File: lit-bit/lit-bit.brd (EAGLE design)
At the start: 8.1 x 1.3 mm, 10 parts, among them IC1 ATMEGA32U4-MU, SW1 SPST_TACT-KMR2, U1 S-1317A33-M5T1U4, X3 microUSB, Y1 8MHz

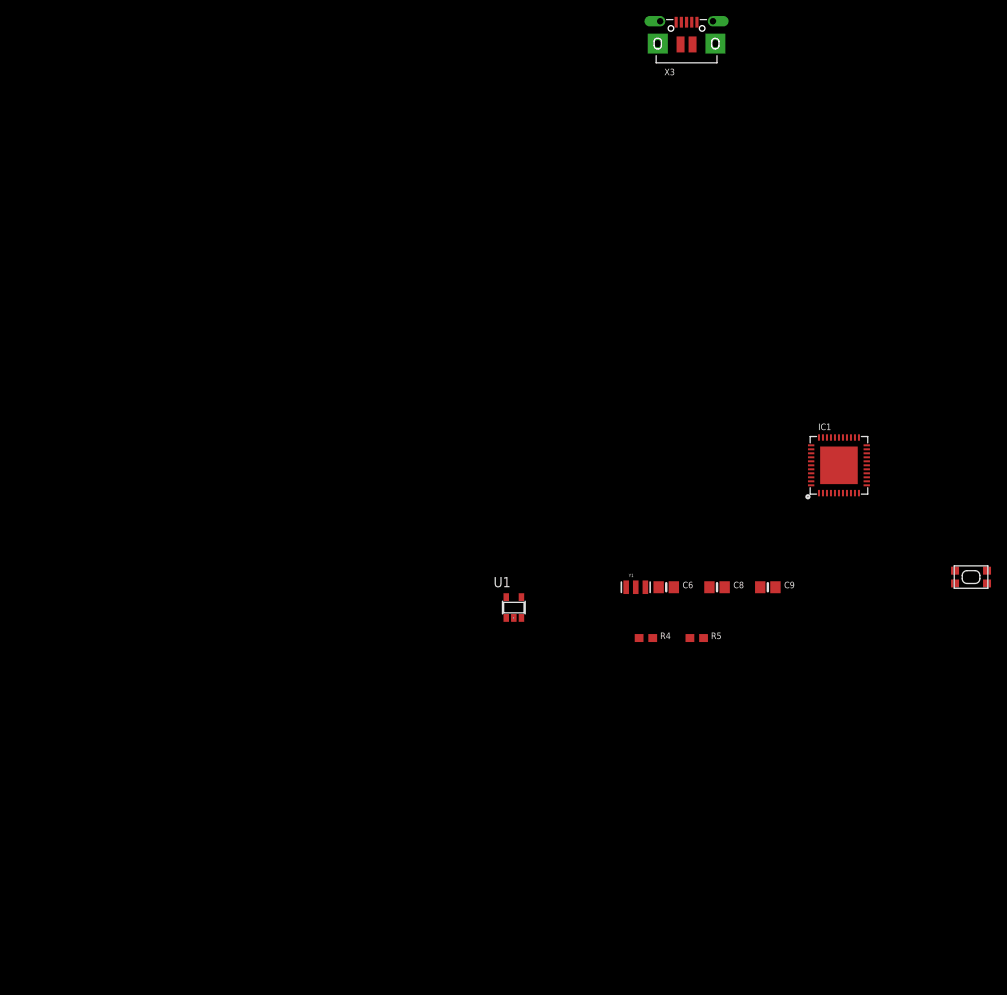
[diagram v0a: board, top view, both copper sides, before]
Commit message: added power circuitry
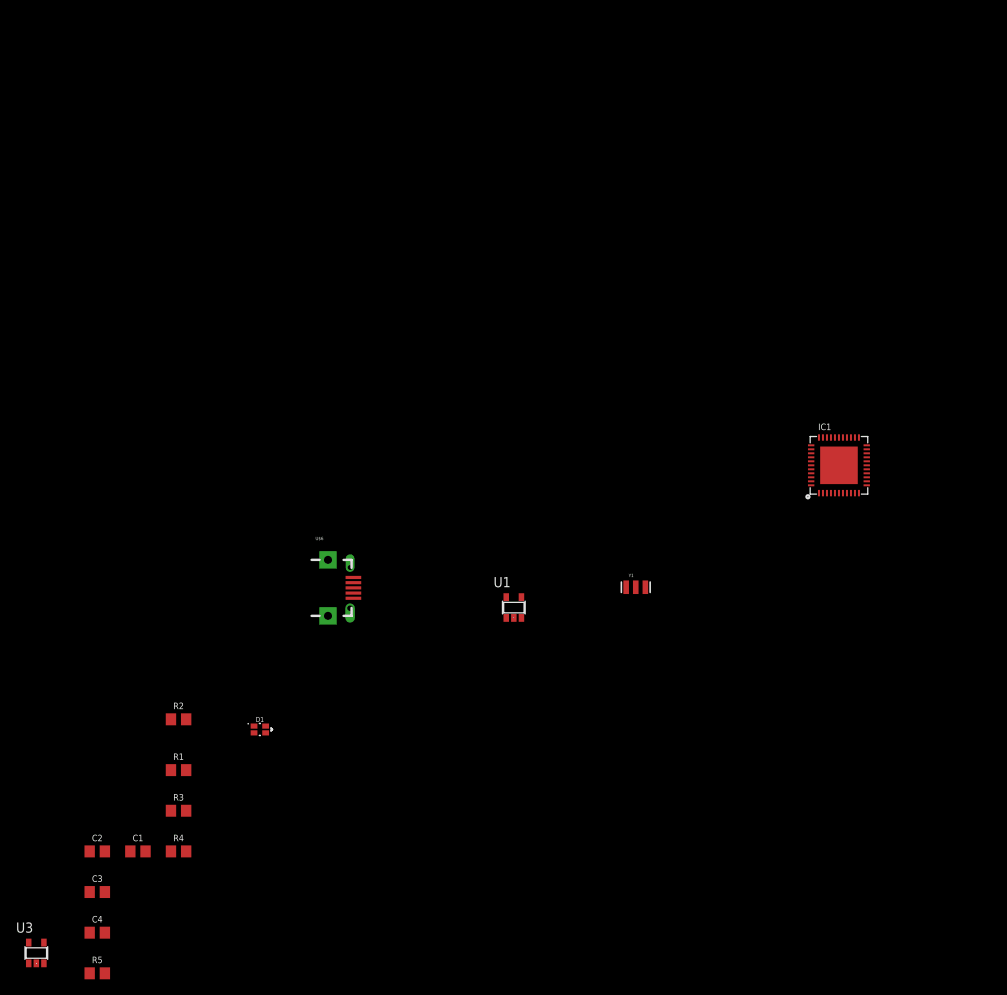
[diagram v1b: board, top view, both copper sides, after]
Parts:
- removed C6, C8: 10µF, microbuilder:0805-NO
- removed C9: 10uF, microbuilder:0805-NO
- removed SW1: SPST_TACT-KMR2, adafruit:KMR2
- removed X3: microUSB, microbuilder:4UCONN_20329_V2
- added C1: 4.7uF, SCADA_CUSTOM_LIBRARY:0805
- added C2, C3, C4: 10uF, SCADA_CUSTOM_LIBRARY:0805
- added D1: LED-RGSMIT, SCADA_CUSTOM_LIBRARY:0606
- added R1: 4700, SCADA_CUSTOM_LIBRARY:0805
- added R2: 150, SCADA_CUSTOM_LIBRARY:0805
- added R3: 22, SCADA_CUSTOM_LIBRARY:0805
- added U$6: USB_MICRO_B_SMD_FEMALE, SCADA_CUSTOM_LIBRARY:USB-B-MICRO-SMD
- added U3: MCP73831T, SCADA_CUSTOM_LIBRARY:SOT23-5
- R4: device microbuilder:0603-NO -> SCADA_CUSTOM_LIBRARY:0805
- R5: value 22 -> 150; device microbuilder:0603-NO -> SCADA_CUSTOM_LIBRARY:0805
- moved R5 85.9 mm to (-55.9, -40.6)
- moved R4 64.2 mm to (-45.7, -25.4)
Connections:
- removed net A0: IC1.36
- removed net A1: IC1.37
- removed net A2: IC1.38
- removed net A3: IC1.39
- removed net A4: IC1.40
- removed net A5: IC1.41
- removed net AREF: IC1.42
- removed net N$15: R5.1, X3.D+
- removed net N$16: R4.1, X3.D-
- new net N$1: IC1.3, R3.2
- new net N$2: R1.1, U3.5
- new net N$3: D1.P$3, R2.2, U3.1
- new net N$4: D1.P$2, R2.1
- new net N$5: D1.P$4, R5.1
- net +3V3: now also C2.2, C4.1; no longer C8.1, C9.1
- net D+: now also R4.1, R4.2, U$6.D+1; no longer R5.2
- net D-: now also R3.1, U$6.D-1; no longer IC1.3, R4.2
- net GND: now also C1.2, C2.1, C3.1, C4.2, IC1.42, R1.2, R5.2, U$6.GND1, U$6.P$1, U$6.P$3, U$6.P$4, U$6.P$5, U3.2; no longer C6.2, C8.2, C9.2, SW1.2, SW1.4, X3.BASE@1, X3.BASE@2, X3.GND, X3.SPRT@1, X3.SPRT@2, X3.SPRT@3, X3.SPRT@4
- net RST: no longer SW1.1, SW1.3
- net VBAT: now also C3.2, U3.3; no longer C6.1
- net VBUS: now also C1.1, D1.P$1, U$6.VBUS1, U3.4; no longer X3.VBUS
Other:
- board outline removed

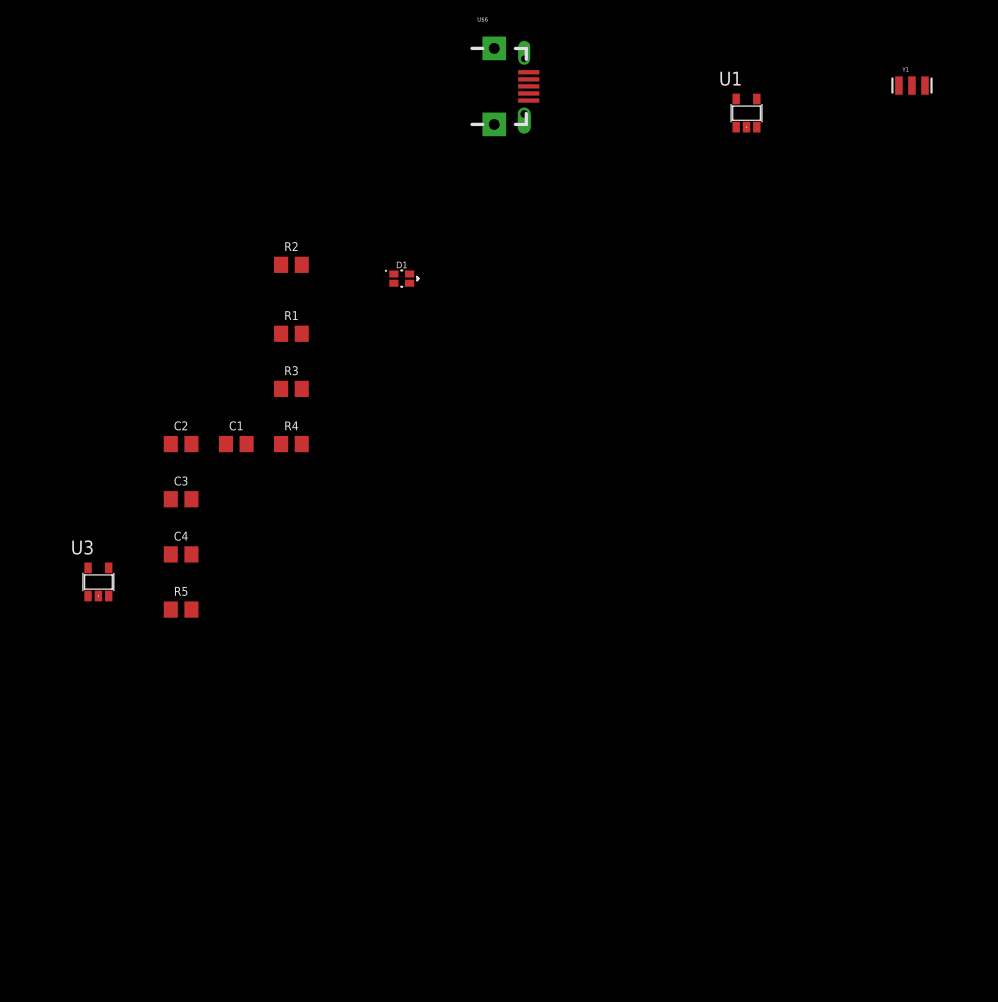
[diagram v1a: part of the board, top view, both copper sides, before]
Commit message: imported TQFN package for 32u4
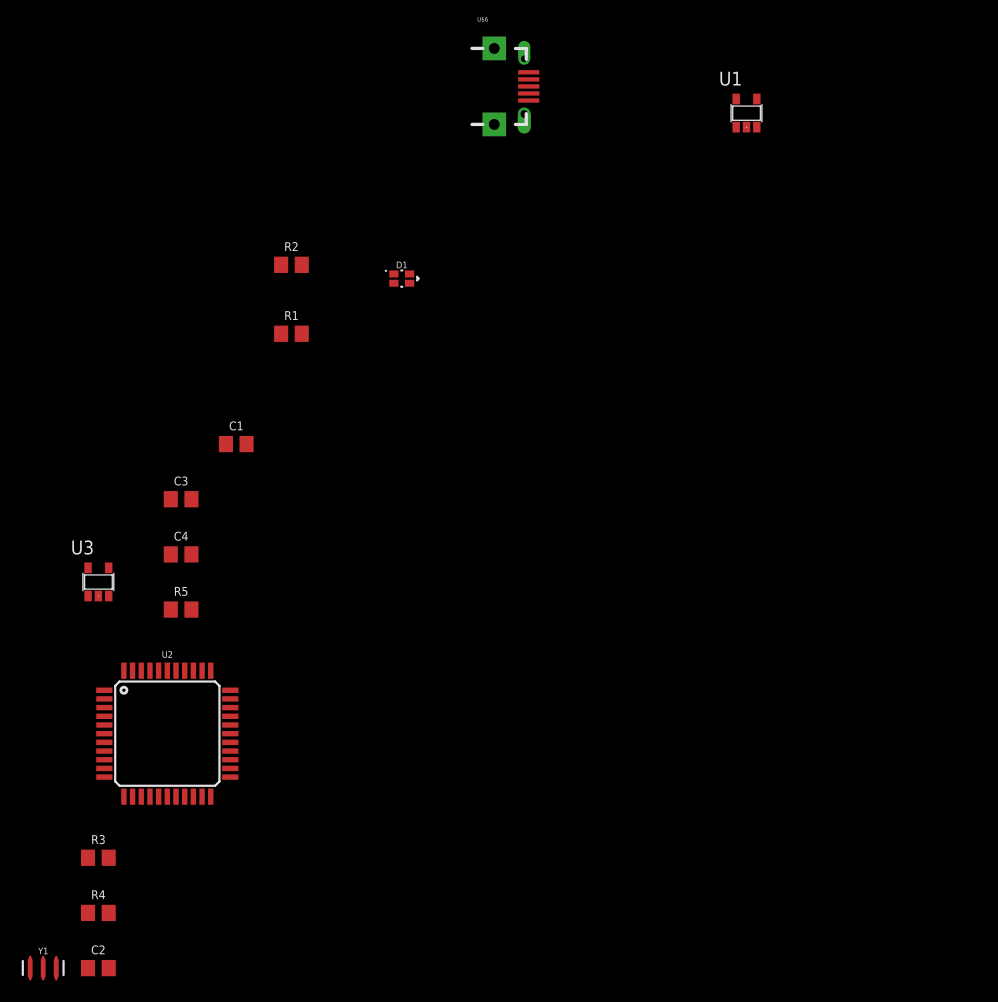
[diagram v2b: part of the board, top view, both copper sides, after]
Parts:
- added U2: 32U4, SCADA_CUSTOM_LIBRARY:TQFP44
- Y1: device SparkFun:RESONATOR-SMD -> SCADA_CUSTOM_LIBRARY:RESONATOR-SMD-3.2X1.3
- moved Y1 114.1 mm to (-68.6, -73.7)
- moved C2 48.9 mm to (-63.5, -73.7)
- moved R3 46.7 mm to (-63.5, -63.5)
- moved R4 46.7 mm to (-63.5, -68.6)
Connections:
- removed net N$11: IC1.16, Y1.3
- removed net N$12: IC1.17, Y1.1
- new net N$6: R3.2, U2.3
- new net N$7: U2.16, Y1.3
- net +3V3: now also U2.14, U2.24, U2.33, U2.34, U2.44, U2.6; no longer IC1.14, IC1.24, IC1.33, IC1.34, IC1.44, IC1.6
- net D+: now also U2.4; no longer IC1.4
- net GND: now also U2.15, U2.23, U2.35, U2.42, U2.43, U2.5; no longer IC1.15, IC1.23, IC1.35, IC1.42, IC1.43, IC1.5
- net MISO: now also U2.11; no longer IC1.11
- net MOSI: now also U2.10; no longer IC1.10
- net N$1: now also U2.17, Y1.1; no longer IC1.3, R3.2
- net RST: now also U2.13; no longer IC1.13
- net SCK: now also U2.9; no longer IC1.9
- net SCL: now also U2.18; no longer IC1.18
- net SDA: now also U2.19; no longer IC1.19
- net VBUS: now also U2.7; no longer IC1.7

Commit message: removed QFN 32u4
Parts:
- removed IC1: ATMEGA32U4-MU, microbuilder:TQFN44_7MM
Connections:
- removed net D0: IC1.20
- removed net D1: IC1.21
- removed net D10: IC1.30
- removed net D11: IC1.12
- removed net D12: IC1.26
- removed net D13: IC1.32
- removed net D4: IC1.25
- removed net D5: IC1.31
- removed net D6: IC1.27
- removed net D7: IC1.1
- removed net D8: IC1.28
- removed net D9: IC1.29
- new net N$10: U2.12
- new net N$11: U2.30
- new net N$12: U2.29
- new net N$13: U2.28
- new net N$14: U2.27
- new net N$15: U2.21
- new net N$16: U2.20
- new net N$17: U2.26
- new net N$18: U2.32
- new net N$19: U2.25
- new net N$8: U2.1
- new net N$9: U2.31
- net GND: now also U2.36, U2.37, U2.38, U2.39, U2.40, U2.41
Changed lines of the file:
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@@
 </autorouter>
 <elements>
-<element name="IC1" library="microbuilder" package="TQFN44_7MM" value="ATMEGA32U4-MU" x="36.83" y="22.86"/>
 <element name="U1" library="SCADA_CUSTOM_LIBRARY" package="SOT23-5" value="S-1317A33-M5T1U4" x="-3.81" y="5.08"/>
 <element name="U$6" library="SCADA_CUSTOM_LIBRARY" package="USB-B-MICRO-SMD" value="USB_MICRO_B_SMD_FEMALE" x="-29.21" y="3.81"/>
@@
 <contactref element="U2" pad="42"/>
 <contactref element="Y1" pad="2"/>
+<contactref element="U2" pad="36"/>
+<contactref element="U2" pad="37"/>
+<contactref element="U2" pad="38"/>
+<contactref element="U2" pad="39"/>
+<contactref element="U2" pad="40"/>
+<contactref element="U2" pad="41"/>
 <wire x1="-64.45" y1="-73.66" x2="-68.58" y2="-73.66" width="0" layer="19" extent="1-1"/>
 <wire x1="-58.75" y1="-57.87" x2="-64.45" y2="-73.66" width="0" layer="19" extent="1-1"/>
@@
 <wire x1="-60.35" y1="-46.27" x2="-62.95" y2="-51.27" width="0" layer="19" extent="1-1"/>
 <wire x1="-59.55" y1="-46.27" x2="-60.35" y2="-46.27" width="0" layer="19" extent="1-1"/>
-<wire x1="-53.95" y1="-46.27" x2="-59.55" y2="-46.27" width="0" layer="19" extent="1-1"/>
-<wire x1="-54.93" y1="-40.64" x2="-53.95" y2="-46.27" width="0" layer="19" extent="1-1"/>
+<wire x1="-58.75" y1="-46.27" x2="-59.55" y2="-46.27" width="0" layer="19" extent="1-1"/>
+<wire x1="-57.95" y1="-46.27" x2="-58.75" y2="-46.27" width="0" layer="19" extent="1-1"/>
+<wire x1="-57.15" y1="-46.27" x2="-57.95" y2="-46.27" width="0" layer="19" extent="1-1"/>
+<wire x1="-56.35" y1="-46.27" x2="-57.15" y2="-46.27" width="0" layer="19" extent="1-1"/>
+<wire x1="-55.55" y1="-46.27" x2="-56.35" y2="-46.27" width="0" layer="19" extent="1-1"/>
+<wire x1="-54.75" y1="-46.27" x2="-55.55" y2="-46.27" width="0" layer="19" extent="1-1"/>
+<wire x1="-53.95" y1="-46.27" x2="-54.75" y2="-46.27" width="0" layer="19" extent="1-1"/>
+<wire x1="-54.93" y1="-40.64" x2="-54.75" y2="-46.27" width="0" layer="19" extent="1-1"/>
 <wire x1="-54.93" y1="-35.56" x2="-54.93" y2="-40.64" width="0" layer="19" extent="1-1"/>
 <wire x1="-56.83" y1="-30.48" x2="-54.93" y2="-35.56" width="0" layer="19" extent="1-1"/>
@@
 <signal name="SDA">
 <contactref element="U2" pad="19"/>
-</signal>
-<signal name="D1">
-<contactref element="IC1" pad="21"/>
-</signal>
-<signal name="D0">
-<contactref element="IC1" pad="20"/>
 </signal>
 <signal name="+3V3">
@@
 <contactref element="U2" pad="18"/>
 </signal>
-<signal name="D4">
-<contactref element="IC1" pad="25"/>
-</signal>
-<signal name="D8">
-<contactref element="IC1" pad="28"/>
-</signal>
-<signal name="D7">
-<contactref element="IC1" pad="1"/>
-</signal>
-<signal name="D5">
-<contactref element="IC1" pad="31"/>
-</signal>
-<signal name="D6">
-<contactref element="IC1" pad="27"/>
-</signal>
-<signal name="D10">
-<contactref element="IC1" pad="30"/>
-</signal>
-<signal name="D12">
-<contactref element="IC1" pad="26"/>
-</signal>
-<signal name="D13">
-<contactref element="IC1" pad="32"/>
-</signal>
-<signal name="D11">
-<contactref element="IC1" pad="12"/>
-</signal>
-<signal name="D9">
-<contactref element="IC1" pad="29"/>
-</signal>
 <signal name="VBAT">
 <contactref element="U1" pad="1"/>
@@
 <contactref element="U2" pad="13"/>
 </signal>
+<signal name="N$9">
+<contactref element="U2" pad="31"/>
+</signal>
+<signal name="N$10">
+<contactref element="U2" pad="12"/>
+</signal>
+<signal name="N$11">
+<contactref element="U2" pad="30"/>
+</signal>
+<signal name="N$12">
+<contactref element="U2" pad="29"/>
+</signal>
+<signal name="N$13">
+<contactref element="U2" pad="28"/>
+</signal>
+<signal name="N$14">
+<contactref element="U2" pad="27"/>
+</signal>
+<signal name="N$8">
+<contactref element="U2" pad="1"/>
+</signal>
+<signal name="N$15">
+<contactref element="U2" pad="21"/>
+</signal>
+<signal name="N$16">
+<contactref element="U2" pad="20"/>
+</signal>
+<signal name="N$17">
+<contactref element="U2" pad="26"/>
+</signal>
+<signal name="N$18">
+<contactref element="U2" pad="32"/>
+</signal>
+<signal name="N$19">
+<contactref element="U2" pad="25"/>
+</signal>
 </signals>

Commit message: Added all the major components to sch working on BLE antenna
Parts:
- removed U$6: USB_MICRO_B_SMD_FEMALE, SCADA_CUSTOM_LIBRARY:USB-B-MICRO-SMD
- added C10, C17, C18, C9: 12pF, SCADA_CUSTOM_LIBRARY:0805
- added C11, C12, C13, C15, C19, C21, C5, C6: 100nF, SCADA_CUSTOM_LIBRARY:0603
- added C14: 10uF, SCADA_CUSTOM_LIBRARY:0603
- added C16: 33nF, SCADA_CUSTOM_LIBRARY:0603
- added C20: 2.2nF, SCADA_CUSTOM_LIBRARY:0603
- added C22: 1.8pF, SCADA_CUSTOM_LIBRARY:0603
- added C23: 1.2pF, SCADA_CUSTOM_LIBRARY:0603
- added C24: 1.5pF, SCADA_CUSTOM_LIBRARY:0603
- added C7: 10uF, SCADA_CUSTOM_LIBRARY:0805-POLAR
- added C8: 4.7uF, SCADA_CUSTOM_LIBRARY:0603
- added FB1: MMZ1608B121C, microbuilder:0805
- added J1: (no value), SparkFun-Connectors:JST-2-SMD
- added J2: USB_MICRO_B_SMD_FEMALE, SCADA_CUSTOM_LIBRARY:USB-B-MICRO-SMD
- added J3: ISP, SCADA_CUSTOM_LIBRARY:2X3_SMD_HAND_SOLDER
- added JMP1, JMP2, JMP3: 0R-JUMPA, jump-0r-smd:A0R-JMP
- added JP1: OLED, pinhead:1X04
- added L1: 5.6nH, SCADA_CUSTOM_LIBRARY:0603
- added L2: 8.2nH, SCADA_CUSTOM_LIBRARY:0603
- added L3: 3.9nH, SCADA_CUSTOM_LIBRARY:0603
- added R6, R7: 2.2k, SCADA_CUSTOM_LIBRARY:0603
- added R8: 10k, SCADA_CUSTOM_LIBRARY:0603
- added R9: 22k, SCADA_CUSTOM_LIBRARY:0603
- added U$28: (no value), microbuilder:ANT_PCB_2.4GHZ_NRF8001_1.6MM_1OZ
- added U4: ADXL345, SCADA_CUSTOM_LIBRARY:LGA-14
- added U5: S-1335M33, SCADA_CUSTOM_LIBRARY:SOT23-5
- added U6: MCP7940N, SCADA_CUSTOM_LIBRARY:8-SOIC_HAND_SOLDER
- added U7: 24FC1025, SCADA_CUSTOM_LIBRARY:8-SOIC_HAND_SOLDER
- added Y2, Y3: 32.768kHz, SCADA_CUSTOM_LIBRARY:CRYSTAL_8X3.8
- C1, C2, R2, R3, R4, R5: device SCADA_CUSTOM_LIBRARY:0805 -> SCADA_CUSTOM_LIBRARY:0603
- C3, C4: value 10uF -> 1uF; device SCADA_CUSTOM_LIBRARY:0805 -> SCADA_CUSTOM_LIBRARY:0603
- R1: value 4700 -> 4.7k; device SCADA_CUSTOM_LIBRARY:0805 -> SCADA_CUSTOM_LIBRARY:0603
- U1: value S-1317A33-M5T1U4 -> (none); device SCADA_CUSTOM_LIBRARY:SOT23-5 -> SCADA_CUSTOM_LIBRARY:QFN32_5MM
- moved U1 140.9 mm to (-82.5, -111.8)
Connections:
- removed net VBUS: C1.1, D1.P$1, U$6.VBUS1, U2.7, U3.4
- new net ACTIVE: U1.6
- new net ADXL-INT: U2.21, U4.8
- new net AVDD: U1.24, U1.26, U1.29
- new net N$20: C9.2, U6.1, Y2.P$1
- new net N$21: C10.2, U6.2, Y2.P$4
- new net N$22: C16.2, U1.3
- new net N$23: C18.2, U1.5, Y3.P$4
- new net N$24: C20.1, L1.2, U1.20
- new net N$25: L1.1, L2.1, U1.21
- new net N$26: J3.2
- new net N$27: JMP1.2, U1.11
- new net N$28: L2.2, L3.1, U1.22
- new net N$29: JMP2.2, U1.13
- new net N$31: C22.2, L3.2
- new net N$32: C22.1, C23.1, C24.1, U$28.FEED
- new net N$34: JMP3.2, U1.14
- new net NRF-RST: U1.19
- new net RDYN: U1.16
- new net REQN: U1.12
- new net RTC-INT: R8.1, U2.20, U6.7
- new net VSS: U1.23, U1.30, U1.31
- new net VUSB: D1.P$1, U2.7
- net +3V3: now also C11.2, C12.2, C13.1, C14.2, C19.2, C21.2, C5.2, C6.1, C7.1, JP1.2, R6.1, R7.1, R8.2, U1.1, U1.9, U4.1, U4.6, U4.7, U5.5, U6.3, U6.8, U7.3, U7.8; no longer U1.5
- net D+: now also J2.D+1; no longer U$6.D+1
- net D-: now also J2.D-1; no longer U$6.D-1
- net GND: now also C10.1, C11.1, C12.1, C13.2, C14.1, C15.1, C16.1, C17.1, C18.1, C19.1, C20.2, C21.1, C23.2, C24.2, C5.1, C6.2, C7.2, C8.2, C9.1, J1.2, J2.GND1, J2.P$1, J2.P$3, J2.P$4, J2.P$5, J3.6, JMP1.3, JMP2.3, JMP3.3, JP1.1, U1.17, U1.18, U1.33, U1.8, U4.12, U4.2, U4.4, U4.5, U5.2, U6.4, U7.1, U7.2, U7.4, U7.7; no longer U$6.GND1, U$6.P$1, U$6.P$3, U$6.P$4, U$6.P$5, U1.2
- net MISO: now also J3.1, JMP3.1
- net MOSI: now also J3.4, JMP2.1
- net N$15: now also C17.2, U1.4, Y3.P$1; no longer U2.21
- net N$16: now also C15.2, U1.2; no longer U2.20
- net RST: now also J3.5
- net SCK: now also J3.3, JMP1.1
- net SCL: now also JP1.4, R7.2, U4.14, U6.6, U7.6
- net SDA: now also JP1.3, R6.2, U4.13, U6.5, U7.5
- net VBAT: now also C1.1, C8.1, J1.1, J2.VBUS1, U3.4, U5.1, U5.3; no longer U1.1

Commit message: finished the schematic starting on the brd now
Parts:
- removed JMP1, JMP2, JMP3: 0R-JUMPA, jump-0r-smd:A0R-JMP
- added 3V3, SCL, SDA, VBAT: LSP10, solpad:LSP10
- added C25, C26: 100nF, SCADA_CUSTOM_LIBRARY:0603
- added C27: 1uF, SCADA_CUSTOM_LIBRARY:0603
- added C28, C29: 16pF, SCADA_CUSTOM_LIBRARY:0603
- added J4, J5: (no value), SparkFun-Connectors:1X02
- added L4: 15nH, SCADA_CUSTOM_LIBRARY:0603
- added L5: 10uH, SCADA_CUSTOM_LIBRARY:0603
- added SJ1, SJ2, SJ3: (no value), microbuilder:SOLDERJUMPER_WAVE
- added Y4: 16MHz, SCADA_CUSTOM_LIBRARY:CRYSTAL_3.2X2.5
- moved J1 426.1 mm to (106.7, 264.2)
- moved L2 426.1 mm to (36.8, 110.5)
- moved U4 426.1 mm to (54.6, 223.5)
- moved C1 426.1 mm to (149.9, 350.5)
- moved C10 426.1 mm to (90.2, 245.1)
- moved C11 426.1 mm to (52.1, 217.2)
- moved C12 426.1 mm to (52.1, 204.5)
- moved C13 426.1 mm to (52.1, 199.4)
- moved C14 426.1 mm to (52.1, 180.3)
- moved C15 426.1 mm to (52.1, 176.5)
- moved C16 426.1 mm to (52.1, 172.7)
- moved C17 426.1 mm to (52.1, 157.5)
- moved C18 426.1 mm to (52.1, 152.4)
- moved C19 426.1 mm to (52.1, 147.3)
- moved C2 426.1 mm to (137.2, 302.3)
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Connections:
- removed net VSS: U1.23, U1.30, U1.31
- new net 3V3: FB1.1, J5.1
- new net N$30: R9.2, U1.25
- new net N$33: C28.2, U1.28, Y4.2
- new net N$35: L4.1, L5.2
- new net N$36: L5.1, U1.32
- new net N$37: C29.2, U1.27, Y4.1
- new net N$41: C3.2, J4.2, U5.1, U5.3
- net +3V3: now also 3V3.MP, J5.2
- net AVDD: now also C25.2, C26.1, C27.1, FB1.2, L4.2
- net GND: now also C25.1, C26.2, C27.2, C28.1, C29.1, R9.1, U1.23, U1.30, U1.31; no longer JMP1.3, JMP2.3, JMP3.3
- net MISO: now also SJ3.1; no longer JMP3.1
- net MOSI: now also SJ2.1; no longer JMP2.1
- net N$27: now also SJ1.2; no longer JMP1.2
- net N$29: now also SJ2.2; no longer JMP2.2
- net N$34: now also SJ3.2; no longer JMP3.2
- net SCK: now also SJ1.1; no longer JMP1.1
- net SCL: now also SCL.MP
- net SDA: now also SDA.MP
- net VBAT: now also J4.1, VBAT.MP; no longer C3.2, U5.1, U5.3
